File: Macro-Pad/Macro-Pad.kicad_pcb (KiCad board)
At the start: 2 copper layers, 14 parts, among them J1 USB_C_Receptacle_USB2.0_14P, U1 ESP32-S3-WROOM-1, U2 TPS62162DSG

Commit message: v2
a lil' smaller than the last one
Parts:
- moved C1 38.5 mm to (36.5, 56.5), turned to -90 degrees
- moved R2 30.3 mm to (36.0, 46.5), turned to -90 degrees
- moved J1 29.2 mm to (50.5, 44.5), turned to 90 degrees
- moved R1 27.5 mm to (38.0, 46.5), turned to -90 degrees
- moved R3 26.4 mm to (35.0, 37.5), turned to 0 degrees
- moved L1 25.5 mm to (37.0, 51.5), turned to 0 degrees
- moved U2 19.0 mm to (37.0, 41.5), turned to 180 degrees
- moved U1 12.6 mm to (44.7, 23.0), turned to 0 degrees
- moved C2 12.5 mm to (42.5, 48.0), turned to 180 degrees
- moved RST1 8.08 mm to (50.0, 61.5), turned to -90 degrees
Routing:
- net Net-(U1-IO42): track 39.8 -> 77.3 mm, vias 2 -> 0
- net Net-(J1-CC2): track 38.7 -> 12.4 mm
- net Net-(U1-3V3): track 47.1 -> 22.5 mm, vias 3 -> 2
- net Net-(J1-SHIELD): track 222.9 -> 243.5 mm, vias 0 -> 1
- net Net-(U1-USB_D-): track 7.19 -> 26.8 mm, vias 0 -> 2
- net Net-(U1-EN): track 6.10 -> 25.3 mm
- net Net-(U1-IO45): track 55.8 -> 74.2 mm, vias 0 -> 2
- net Net-(U1-IO0): track 21.1 -> 32.6 mm, vias 0 -> 2
- net Net-(U1-USB_D+): track 8.33 -> 19.2 mm, vias 0 -> 2
- net Net-(U1-IO40): track 49.3 -> 39.1 mm, vias 2 -> 0
- net Net-(U1-IO41): track 37.4 -> 47.3 mm, vias 1 -> 2
- net Net-(U2-SW): track 5.90 -> 14.9 mm
- net Net-(U2-EN): track 20.8 -> 16.1 mm
- net Net-(J1-CC1): track 8.44 -> 11.1 mm, vias 0 -> 2
- net Net-(U2-AGND): track 8.11 -> 7.29 mm

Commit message: v2.1
small wiring tweaks to make more compact (not smaller)
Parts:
- moved RST1 4.53 mm to (49.8, 57.0)
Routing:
- net Net-(U1-IO42): track 77.3 -> 66.7 mm, vias 0 -> 2
- net Net-(J1-SHIELD): track 243.5 -> 238.7 mm
- net Net-(U1-IO0): track 32.6 -> 29.0 mm
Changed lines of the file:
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@@
 	(footprint "Button_Switch_SMD:SW_SPST_PTS645Sx43SMTR92"
 		(layer "F.Cu")
-		(at 50 61.5 -90)
+		(at 49.75 56.98 -90)
 		(descr "Tactile switch, 6x6 mm, H4.3 mm, gullwing terminals, https://www.ckswitches.com/media/1471/pts645.pdf")
 		(tags "SPST Button Switch CK C&K")
@@
 	)
 	(segment
+		(start 28.83 16.63)
+		(end 46.63 16.63)
+		(width 0.2)
+		(layer "F.Cu")
+		(net "Net-(J1-SHIELD)")
+	)
+	(segment
 		(start 36.5 56.98)
 		(end 37.225 56.98)
@@
 	)
 	(segment
-		(start 47.75 65.48)
-		(end 47.75 57.52)
+		(start 47.5 60.96)
+		(end 47.5 53)
+		(width 0.2)
+		(layer "F.Cu")
+		(net "Net-(J1-SHIELD)")
+	)
+	(segment
+		(start 47.37 48.82)
+		(end 47.37 52.87)
 		(width 0.2)
 		(layer "F.Cu")
@@
 	)
 	(segment
+		(start 46.63 16.63)
+		(end 50 20)
+		(width 0.2)
+		(layer "F.Cu")
+		(net "Net-(J1-SHIELD)")
+	)
+	(segment
 		(start 46.455 47.905)
 		(end 47.37 48.82)
@@
 	)
 	(segment
-		(start 29.463402 21.86)
-		(end 24.973402 26.35)
-		(width 0.2)
-		(layer "F.Cu")
-		(net "Net-(J1-SHIELD)")
-	)
-	(segment
 		(start 35.4 52.7)
 		(end 35.4 49.925)
@@
 	)
 	(segment
-		(start 18.79 20.880101)
-		(end 20.750101 18.92)
-		(width 0.2)
-		(layer "F.Cu")
-		(net "Net-(J1-SHIELD)")
-	)
-	(segment
 		(start 36 47.325)
 		(end 38 47.325)
@@
 	)
 	(segment
-		(start 34.109088 17.78)
-		(end 30.029087 21.86)
-		(width 0.2)
-		(layer "F.Cu")
-		(net "Net-(J1-SHIELD)")
-	)
-	(segment
 		(start 15 38)
 		(end 15 57.5)
@@
 	)
 	(segment
-		(start 24.973402 26.35)
-		(end 23.026598 26.35)
-		(width 0.2)
-		(layer "F.Cu")
-		(net "Net-(J1-SHIELD)")
-	)
-	(segment
 		(start 35.56 57.92)
 		(end 36.5 56.98)
@@
 	)
 	(segment
+		(start 47.37 52.87)
+		(end 47.5 53)
+		(width 0.2)
+		(layer "F.Cu")
+		(net "Net-(J1-SHIELD)")
+	)
+	(segment
 		(start 54.5 48.5)
 		(end 54.5 40)
@@
 	)
 	(segment
+		(start 26.54 18.92)
+		(end 28.83 16.63)
+		(width 0.2)
+		(layer "F.Cu")
+		(net "Net-(J1-SHIELD)")
+	)
+	(segment
 		(start 36.48 17.78)
 		(end 42.5 23.8)
@@
 	)
 	(segment
-		(start 23.026598 26.35)
-		(end 18.79 22.113402)
-		(width 0.2)
-		(layer "F.Cu")
-		(net "Net-(J1-SHIELD)")
-	)
-	(segment
 		(start 45.25 47.75)
 		(end 45 48)
@@
 	)
 	(segment
-		(start 30.029087 21.86)
-		(end 29.463402 21.86)
-		(width 0.2)
-		(layer "F.Cu")
-		(net "Net-(J1-SHIELD)")
-	)
-	(segment
 		(start 46.455 47.75)
 		(end 41.505 52.7)
@@
 	)
 	(segment
-		(start 47.75 57.52)
-		(end 47.75 49.2)
-		(width 0.2)
-		(layer "F.Cu")
-		(net "Net-(J1-SHIELD)")
-	)
-	(segment
 		(start 47.37 40.335)
 		(end 46.455 41.25)
-		(width 0.2)
-		(layer "F.Cu")
-		(net "Net-(J1-SHIELD)")
-	)
-	(segment
-		(start 18.79 22.113402)
-		(end 18.79 20.880101)
-		(width 0.2)
-		(layer "F.Cu")
-		(net "Net-(J1-SHIELD)")
-	)
-	(segment
-		(start 35.95 17.78)
-		(end 34.109088 17.78)
 		(width 0.2)
 		(layer "F.Cu")
@@
 	)
 	(segment
-		(start 48.7 66.239744)
-		(end 48.7 56.760256)
+		(start 36 59.5)
+		(end 35.5 59.5)
 		(width 0.2)
 		(layer "F.Cu")
@@
 	)
 	(segment
-		(start 41.020256 60.46)
-		(end 47.115256 66.555)
+		(start 34.54 60.46)
+		(end 20.19 60.46)
 		(width 0.2)
 		(layer "F.Cu")
@@
 	)
 	(segment
-		(start 48.384744 66.555)
-		(end 48.7 66.239744)
+		(start 35.5 59.5)
+		(end 34.54 60.46)
 		(width 0.2)
 		(layer "F.Cu")
@@
 	)
 	(segment
-		(start 48.7 56.760256)
-		(end 55.1 50.360256)
-		(width 0.2)
-		(layer "F.Cu")
-		(net "Net-(U1-IO42)")
-	)
-	(segment
-		(start 20.19 60.46)
-		(end 41.020256 60.46)
+		(start 55.1 50.360256)
+		(end 50.139744 50.360256)
 		(width 0.2)
 		(layer "F.Cu")
@@
 		(net "Net-(U1-IO42)")
 	)
-	(segment
-		(start 47.115256 66.555)
-		(end 48.384744 66.555)
-		(width 0.2)
-		(layer "F.Cu")
+	(via
+		(at 50.139744 50.360256)
+		(size 0.6)
+		(drill 0.3)
+		(layers "F.Cu" "B.Cu")
+		(net "Net-(U1-IO42)")
+	)
+	(via
+		(at 36 59.5)
+		(size 0.6)
+		(drill 0.3)
+		(layers "F.Cu" "B.Cu")
+		(net "Net-(U1-IO42)")
+	)
+	(segment
+		(start 50.139744 50.360256)
+		(end 45.139744 50.360256)
+		(width 0.2)
+		(layer "B.Cu")
+		(net "Net-(U1-IO42)")
+	)
+	(segment
+		(start 45.139744 50.360256)
+		(end 36 59.5)
+		(width 0.2)
+		(layer "B.Cu")
 		(net "Net-(U1-IO42)")
 	)
@@
 	)
 	(segment
-		(start 52.25 57.52)
-		(end 52.25 54.25)
+		(start 53 53)
+		(end 52 53)
 		(width 0.2)
 		(layer "F.Cu")
@@
 	)
 	(segment
-		(start 52.25 57.52)
-		(end 52.25 65.48)
+		(start 54.5 52)
+		(end 54 52)
+		(width 0.2)
+		(layer "F.Cu")
+		(net "Net-(U1-IO0)")
+	)
+	(segment
+		(start 52 53)
+		(end 52 60.96)
 		(width 0.2)
 		(layer "F.Cu")
@@
 		(net "Net-(U1-IO0)")
 	)
-	(via
-		(at 52.25 54.25)
-		(size 0.6)
-		(drill 0.3)
-		(layers "F.Cu" "B.Cu")
+	(segment
+		(start 54 52)
+		(end 53 53)
+		(width 0.2)
+		(layer "F.Cu")
 		(net "Net-(U1-IO0)")
 	)
@@
 		(net "Net-(U1-IO0)")
 	)
+	(via
+		(at 54.5 52)
+		(size 0.6)
+		(drill 0.3)
+		(layers "F.Cu" "B.Cu")
+		(net "Net-(U1-IO0)")
+	)
 	(segment
 		(start 54.5 52)
@@
 		(width 0.2)
 		(layer "B.Cu")
-		(net "Net-(U1-IO0)")
-	)
-	(segment
-		(start 52.25 54.25)
-		(end 54.5 52)
-		(width 0.2)
-		(layer "B.Cu")

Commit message: v2.3
bug fix, i forgot to map 2 traces, lol
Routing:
- net Net-(U1-3V3): track 22.5 -> 52.5 mm, vias 2 -> 6
- net Net-(U1-EN): track 25.3 -> 43.8 mm
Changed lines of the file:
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@@
+	)
+	(segment
+		(start 34.175 37.5)
+		(end 34.175 21.145)
+		(width 0.2)
+		(layer "F.Cu")
+		(net "Net-(U1-EN)")
 	)
 	(segment
@@
 	)
 	(segment
+		(start 34.175 21.145)
+		(end 35 20.32)
+		(width 0.2)
+		(layer "F.Cu")
+		(net "Net-(U1-EN)")
+	)
+	(segment
 		(start 36.5 56.02)
 		(end 32.52 56.02)
@@
 		(start 32.52 56.02)
 		(end 31.5 55)
+		(width 0.2)
+		(layer "F.Cu")
+		(net "Net-(U1-EN)")
+	)
+	(segment
+		(start 35 20.32)
+		(end 35.95 20.32)
 		(width 0.2)
 		(layer "F.Cu")
@@
 	)
 	(segment
+		(start 35.669928 41.25)
+		(end 34.5 40.080072)
+		(width 0.2)
+		(layer "F.Cu")
+		(net "Net-(U1-3V3)")
+	)
+	(segment
 		(start 38 49.6)
 		(end 37.6 50)
@@
 	)
 	(segment
+		(start 32.5 36)
+		(end 32.5 21.55)
+		(width 0.2)
+		(layer "F.Cu")
+		(net "Net-(U1-3V3)")
+	)
+	(segment
 		(start 36.1 51.5)
 		(end 37.6 50)
@@
 	)
 	(segment
+		(start 37 38)
+		(end 37 37.5)
+		(width 0.2)
+		(layer "F.Cu")
+		(net "Net-(U1-3V3)")
+	)
+	(segment
 		(start 42.02 48)
 		(end 41 48)
@@
 	)
 	(segment
+		(start 34.5 40.080072)
+		(end 34.5 40)
+		(width 0.2)
+		(layer "F.Cu")
+		(net "Net-(U1-3V3)")
+	)
+	(segment
+		(start 37 37.5)
+		(end 35.825 37.5)
+		(width 0.2)
+		(layer "F.Cu")
+		(net "Net-(U1-3V3)")
+	)
+	(segment
 		(start 35.669928 41.25)
 		(end 36.05 41.25)
@@
 	)
 	(segment
+		(start 35 19.05)
+		(end 35.95 19.05)
+		(width 0.2)
+		(layer "F.Cu")
+		(net "Net-(U1-3V3)")
+	)
+	(segment
+		(start 32.5 21.55)
+		(end 35 19.05)
+		(width 0.2)
+		(layer "F.Cu")
+		(net "Net-(U1-3V3)")
+	)
+	(segment
 		(start 38.5 50)
 		(end 39 49.5)
@@
 	)
 	(segment
+		(start 35.825 37.5)
+		(end 35.825 36.825)
+		(width 0.2)
+		(layer "F.Cu")
+		(net "Net-(U1-3V3)")
+	)
+	(segment
 		(start 38 48.5)
 		(end 38 49.6)
+		(width 0.2)
+		(layer "F.Cu")
+		(net "Net-(U1-3V3)")
+	)
+	(segment
+		(start 35.825 36.825)
+		(end 35 36)
 		(width 0.2)
 		(layer "F.Cu")
@@
 		(net "Net-(U1-3V3)")
 	)
+	(via
+		(at 37 38)
+		(size 0.6)
+		(drill 0.3)
+		(layers "F.Cu" "B.Cu")
+		(net "Net-(U1-3V3)")
+	)
+	(via
+		(at 32.5 36)
+		(size 0.6)
+		(drill 0.3)
+		(layers "F.Cu" "B.Cu")
+		(net "Net-(U1-3V3)")
+	)
+	(via
+		(at 34.5 40)
+		(size 0.6)
+		(drill 0.3)
+		(layers "F.Cu" "B.Cu")
+		(net "Net-(U1-3V3)")
+	)
+	(via
+		(at 35 36)
+		(size 0.6)
+		(drill 0.3)
+		(layers "F.Cu" "B.Cu")
+		(net "Net-(U1-3V3)")
+	)
 	(segment
 		(start 38.5 48)
@@
 	)
 	(segment
+		(start 35 36)
+		(end 32.5 36)
+		(width 0.2)
+		(layer "B.Cu")
+		(net "Net-(U1-3V3)")
+	)
+	(segment
+		(start 36.5 38)
+		(end 37 38)
+		(width 0.2)
+		(layer "B.Cu")
+		(net "Net-(U1-3V3)")
+	)
+	(segment
 		(start 41 48)
 		(end 38.5 48)
 		(width 0.2)
 		(layer "B.Cu")
+		(net "Net-(U1-3V3)")
+	)
+	(segment
+		(start 34.5 40)
+		(end 36.5 38)
+		(width 0.2)
+		(layer "B.Cu")

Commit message: i forgot my ypdatesa
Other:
- board text added: "@Kyguyog"
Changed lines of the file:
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@@
 		)
 		(property "Value" "TPS62162DSG"
-			(at -36.925 1.015 90)
+			(at 2.5 -4 90)
 			(layer "F.Fab")
 			(effects
@@
 			(at 0 4.15 90)
 			(layer "F.Fab")
+			(hide yes)
 			(effects
 				(font
@@
 		)
 	)
+	(gr_text "@Kyguyog"
+		(at 34.5 62 0)
+		(layer "F.Cu")
+		(effects
+			(font
+				(size 1.5 1.5)
+				(thickness 0.3)
+				(bold yes)
+			)
+			(justify left bottom)
+		)
+	)
+	(barcode
+		(at 43.625 72.125 0)
+		(layer "F.Cu")
+		(size 17.75 17.75)
+		(text "https://github.com/Kyguyog")
+		(text_height 1.5)
+		(type qr)
+		(ecc_level L)
+		(hide yes)
+		(knockout no)
+	)
+	(barcode
+		(at 52.5 76 0)
+		(layer "F.Cu")
+		(size 10 10)
+		(text "")
+		(text_height 1.5)
+		(type qr)
+		(ecc_level L)
+		(hide no)
+		(knockout no)
+	)
 	(segment

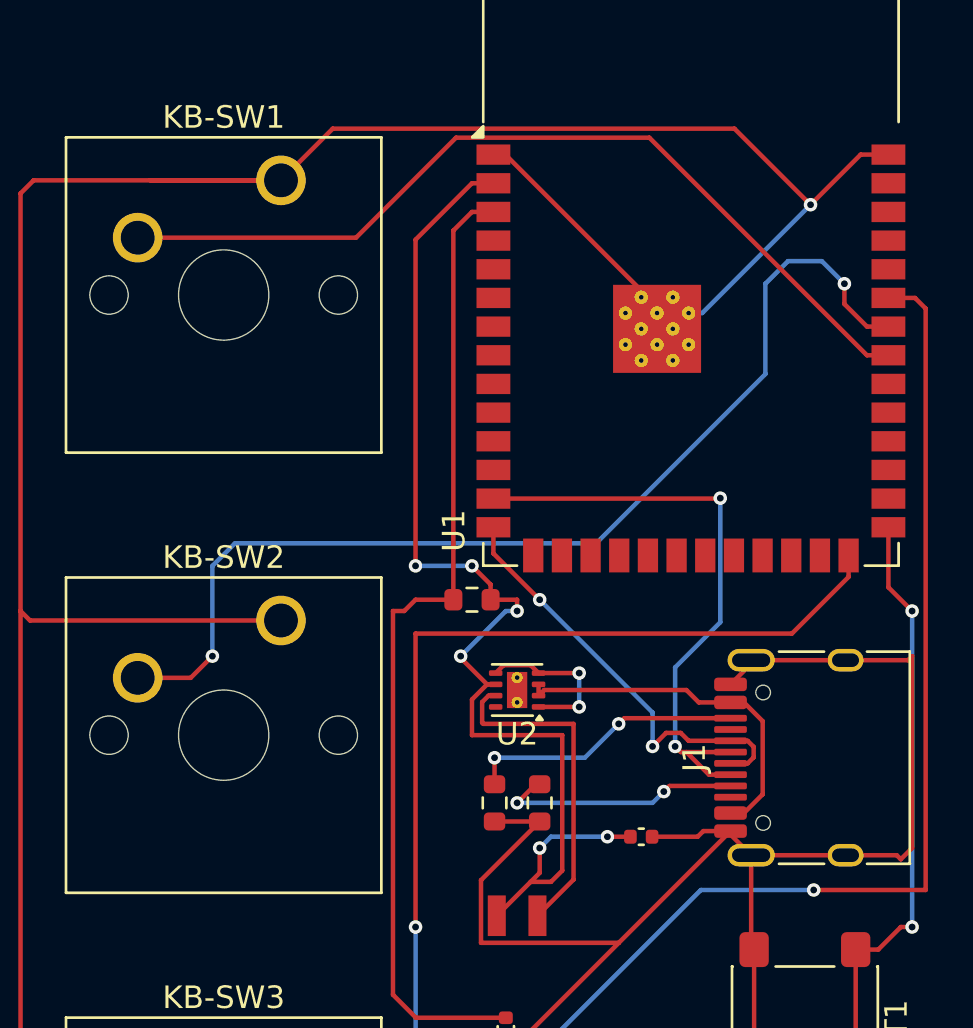
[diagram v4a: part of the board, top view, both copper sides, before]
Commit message: fix outdated pcb wiring
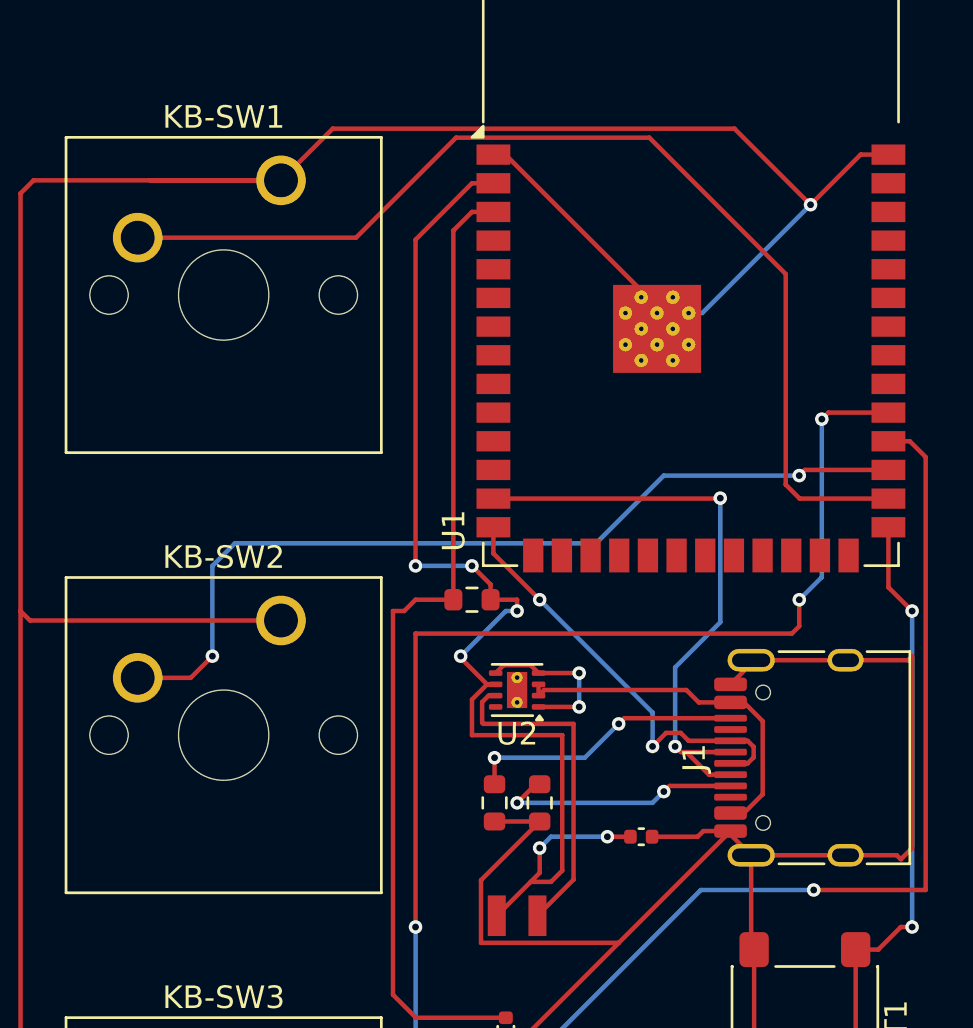
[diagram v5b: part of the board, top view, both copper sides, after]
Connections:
- KB-SW1 pad 2: Net-(U1-IO40) -> Net-(U1-IO35)
- KB-SW2 pad 2: Net-(U1-IO41) -> Net-(U1-IO36)
- KB-SW3 pad 2: Net-(U1-IO42) -> Net-(U1-IO37)
- KB-SW4 pad 2: Net-(U1-IO45) -> Net-(U1-IO38)
- U1 pad 26: Net-(U1-IO45) -> unconnected-(U1-IO45-Pad26)
- U1 pad 28: unconnected-(U1-IO35-Pad28) -> Net-(U1-IO35)
- U1 pad 29: unconnected-(U1-IO36-Pad29) -> Net-(U1-IO36)
- U1 pad 30: unconnected-(U1-IO37-Pad30) -> Net-(U1-IO37)
- U1 pad 31: unconnected-(U1-IO38-Pad31) -> Net-(U1-IO38)
- U1 pad 33: Net-(U1-IO40) -> unconnected-(U1-IO40-Pad33)
- U1 pad 34: Net-(U1-IO41) -> unconnected-(U1-IO41-Pad34)
- U1 pad 35: Net-(U1-IO42) -> unconnected-(U1-IO42-Pad35)
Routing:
- net Net-(U1-IO38): track 0.00 -> 82.8 mm, vias 0 -> 4
- net Net-(U1-IO45): track 74.2 -> 0.00 mm, vias 2 -> 0
- net Net-(U1-IO42): track 66.7 -> 0.00 mm, vias 2 -> 0
- net Net-(U1-IO37): track 0.00 -> 60.2 mm, vias 0 -> 2
- net Net-(U1-IO41): track 47.3 -> 0.00 mm, vias 2 -> 0
- net Net-(U1-IO35): track 0.00 -> 47.2 mm
- net Net-(U1-IO36): track 0.00 -> 39.4 mm, vias 0 -> 2
- net Net-(U1-IO40): track 39.1 -> 0.00 mm

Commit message: change btn name, move traces
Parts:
- renumbered RST1 to BOOT1
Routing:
- net Net-(J1-SHIELD): track 238.7 -> 234.0 mm
- net Net-(U1-IO37): track 60.2 -> 57.5 mm, vias 2 -> 4
- net Net-(U1-IO0): track 29.0 -> 27.3 mm, vias 2 -> 0
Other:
- board outline added: 42 x 80.5 mm
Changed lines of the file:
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@@
 		(descr "Tactile switch, 6x6 mm, H4.3 mm, gullwing terminals, https://www.ckswitches.com/media/1471/pts645.pdf")
 		(tags "SPST Button Switch CK C&K")
-		(property "Reference" "RST1"
+		(property "Reference" "BOOT1"
 			(at 0 -4.05 90)
 			(layer "F.SilkS")
@@
 		)
 	)
+	(gr_rect
+		(start 13 13)
+		(end 55 93.5)
+		(stroke
+			(width 0.05)
+			(type default)
+		)
+		(fill no)
+		(layer "Edge.Cuts")
+	)
 	(gr_text "@Kyguyog"
 		(at 34.5 62 0)
@@
 	)
 	(segment
+		(start 47.92 40.18)
+		(end 48.62 40.88)
+		(width 0.2)
+		(layer "F.Cu")
+		(net "Net-(J1-SHIELD)")
+	)
+	(segment
 		(start 46.455 47.75)
 		(end 46.455 47.905)
@@
 	)
 	(segment
+		(start 48.62 47.624594)
+		(end 47.424594 48.82)
+		(width 0.2)
+		(layer "F.Cu")
+		(net "Net-(J1-SHIELD)")
+	)
+	(segment
 		(start 36 47.325)
 		(end 38 47.325)
@@
 	)
 	(segment
-		(start 54.32 40.18)
-		(end 51.55 40.18)
+		(start 47.37 40.18)
+		(end 47.92 40.18)
 		(width 0.2)
 		(layer "F.Cu")
@@
 	)
 	(segment
-		(start 54.5 40)
-		(end 54.32 40.18)
-		(width 0.2)
-		(layer "F.Cu")
-		(net "Net-(J1-SHIELD)")
-	)
-	(segment
 		(start 26.5 19.5)
 		(end 27 19.5)
@@
 	)
 	(segment
-		(start 54.5 48.5)
-		(end 54.5 40)
-		(width 0.2)
-		(layer "F.Cu")
-		(net "Net-(J1-SHIELD)")
-	)
-	(segment
-		(start 51.55 48.82)
-		(end 53.82 48.82)
+		(start 47.424594 48.82)
+		(end 47.37 48.82)
 		(width 0.2)
 		(layer "F.Cu")
@@
 	)
 	(segment
-		(start 53.82 48.82)
-		(end 54 49)
-		(width 0.2)
-		(layer "F.Cu")
-		(net "Net-(J1-SHIELD)")
-	)
-	(segment
 		(start 47.37 48.82)
 		(end 51.55 48.82)
@@
 	)
 	(segment
-		(start 54 49)
-		(end 54.5 48.5)
-		(width 0.2)
-		(layer "F.Cu")
-		(net "Net-(J1-SHIELD)")
-	)
-	(segment
 		(start 47.37 40.18)
 		(end 47.37 40.335)
@@
 		(start 15.42 57.92)
 		(end 26.54 57.92)
+		(width 0.2)
+		(layer "F.Cu")
+		(net "Net-(J1-SHIELD)")
+	)
+	(segment
+		(start 48.62 40.88)
+		(end 48.62 47.624594)
 		(width 0.2)
 		(layer "F.Cu")
@@
 	)
 	(segment
-		(start 53.45 36.95)
+		(start 52 53)
+		(end 53.45 51.55)
+		(width 0.2)
+		(layer "F.Cu")
+		(net "Net-(U1-IO0)")
+	)
+	(segment
+		(start 53.45 51.55)
 		(end 53.45 34.29)
-		(width 0.2)
-		(layer "F.Cu")
-		(net "Net-(U1-IO0)")
-	)
-	(segment
-		(start 53 53)
-		(end 52 53)
-		(width 0.2)
-		(layer "F.Cu")
-		(net "Net-(U1-IO0)")
-	)
-	(segment
-		(start 54.5 52)
-		(end 54 52)
 		(width 0.2)
 		(layer "F.Cu")
@@
 		(width 0.2)
 		(layer "F.Cu")
-		(net "Net-(U1-IO0)")
-	)
-	(segment
-		(start 54.5 38)
-		(end 53.45 36.95)
-		(width 0.2)
-		(layer "F.Cu")
-		(net "Net-(U1-IO0)")
-	)
-	(segment
-		(start 54 52)
-		(end 53 53)
-		(width 0.2)
-		(layer "F.Cu")
-		(net "Net-(U1-IO0)")
-	)
-	(via
-		(at 54.5 38)
-		(size 0.6)
-		(drill 0.3)
-		(layers "F.Cu" "B.Cu")
-		(net "Net-(U1-IO0)")
-	)
-	(via
-		(at 54.5 52)
-		(size 0.6)
-		(drill 0.3)
-		(layers "F.Cu" "B.Cu")
-		(net "Net-(U1-IO0)")
-	)
-	(segment
-		(start 54.5 52)
-		(end 54.5 38)
-		(width 0.2)
-		(layer "B.Cu")
 		(net "Net-(U1-IO0)")
 	)
@@
 	)
 	(segment
+		(start 52.65 49.151371)
+		(end 52.65 39.15)
+		(width 0.2)
+		(layer "F.Cu")
+		(net "Net-(U1-IO37)")
+	)
+	(segment
+		(start 52 30.5)
+		(end 53.43 30.5)
+		(width 0.2)
+		(layer "F.Cu")
+		(net "Net-(U1-IO37)")
+	)
+	(segment
+		(start 51.441115 50.360256)
+		(end 52.65 49.151371)
+		(width 0.2)
+		(layer "F.Cu")
+		(net "Net-(U1-IO37)")
+	)
+	(segment
 		(start 35.5 59.5)
 		(end 34.54 60.46)
@@
 	)
 	(segment
-		(start 54.4 30.48)
+		(start 52.65 39.15)
+		(end 52 38.5)
+		(width 0.2)
+		(layer "F.Cu")
+		(net "Net-(U1-IO37)")
+	)
+	(segment
+		(start 50.139744 50.360256)
+		(end 51.441115 50.360256)
+		(width 0.2)
+		(layer "F.Cu")
+		(net "Net-(U1-IO37)")
+	)
+	(segment
+		(start 53.43 30.5)
 		(end 53.45 30.48)
-		(width 0.2)
-		(layer "F.Cu")
-		(net "Net-(U1-IO37)")
-	)
-	(segment
-		(start 55.1 50.360256)
-		(end 50.139744 50.360256)
-		(width 0.2)
-		(layer "F.Cu")
-		(net "Net-(U1-IO37)")
-	)
-	(segment
-		(start 55.1 50.360256)
-		(end 55.1 31.18)
-		(width 0.2)
-		(layer "F.Cu")
-		(net "Net-(U1-IO37)")
-	)
-	(segment
-		(start 55.1 31.18)
-		(end 54.4 30.48)
 		(width 0.2)
 		(layer "F.Cu")
@@
 	)
 	(via
+		(at 52 38.5)
+		(size 0.6)
+		(drill 0.3)
+		(layers "F.Cu" "B.Cu")
+		(net "Net-(U1-IO37)")
+	)
+	(via
+		(at 52 30.5)
+		(size 0.6)
+		(drill 0.3)
+		(layers "F.Cu" "B.Cu")
+		(net "Net-(U1-IO37)")
+	)
+	(via
 		(at 36 59.5)
 		(size 0.6)
@@
 		(width 0.2)
 		(layer "B.Cu")
+		(net "Net-(U1-IO37)")
+	)
+	(segment
+		(start 52 38.5)
+		(end 52 30.5)
+		(width 0.2)
+		(layer "B.Cu")
